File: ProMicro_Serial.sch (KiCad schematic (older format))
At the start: 48 parts, among them J1 USB_C_Receptacle_USB2.0, J2 Conn_01x06, U1 FT232H, U2 93CxxB, Y1 12Mhz

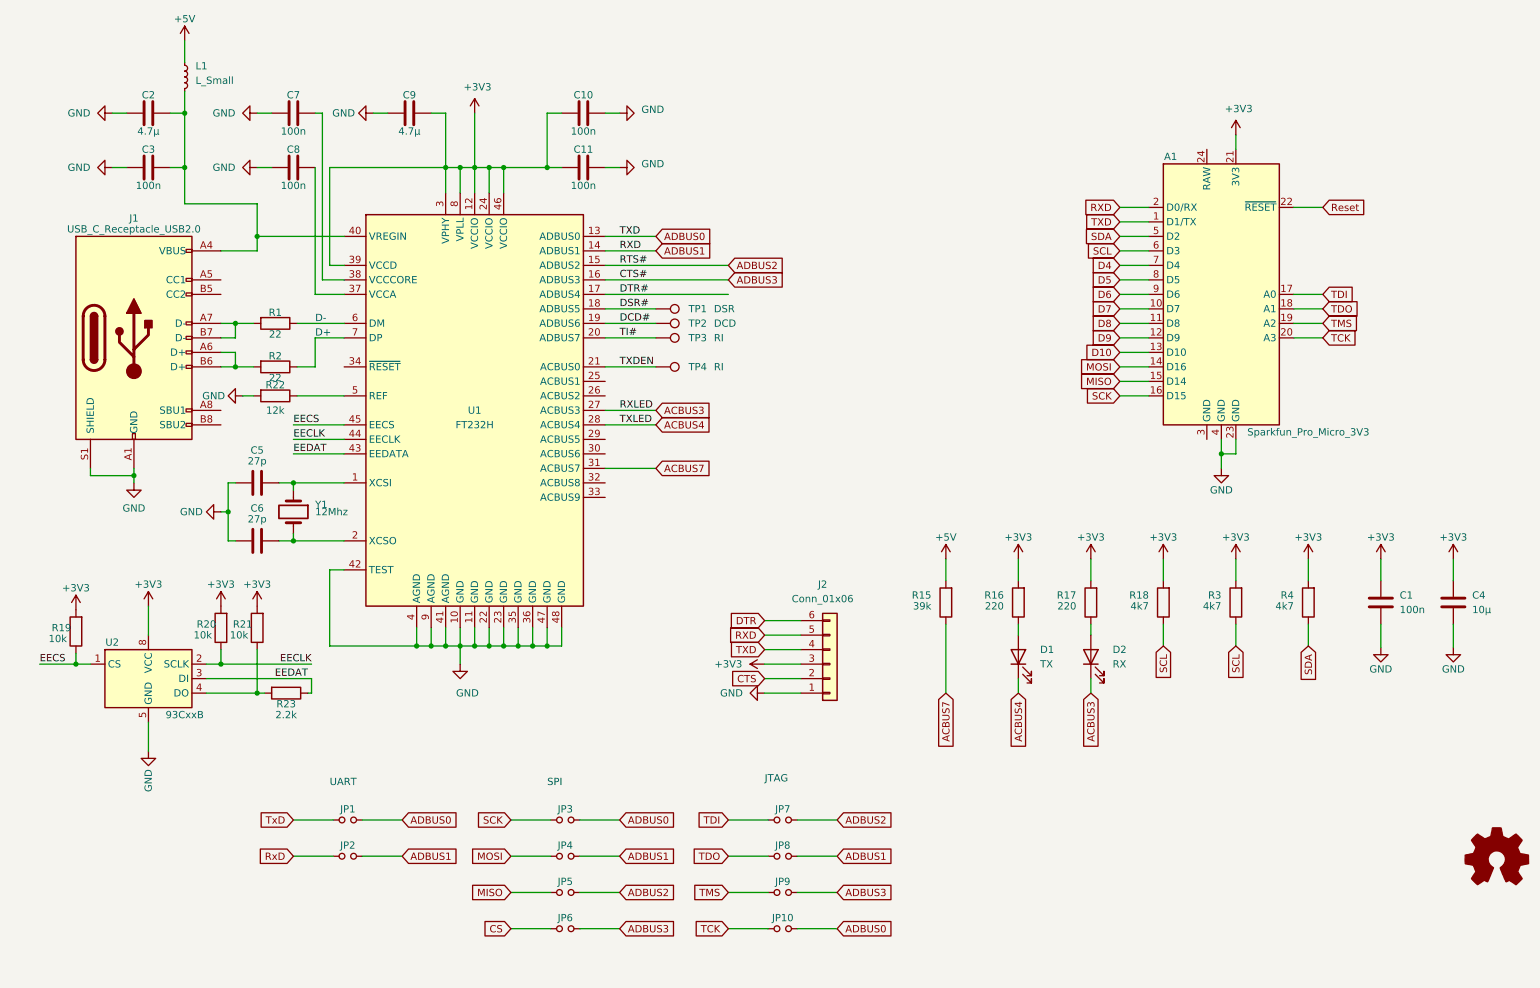
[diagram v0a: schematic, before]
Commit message: schematic, placed parts
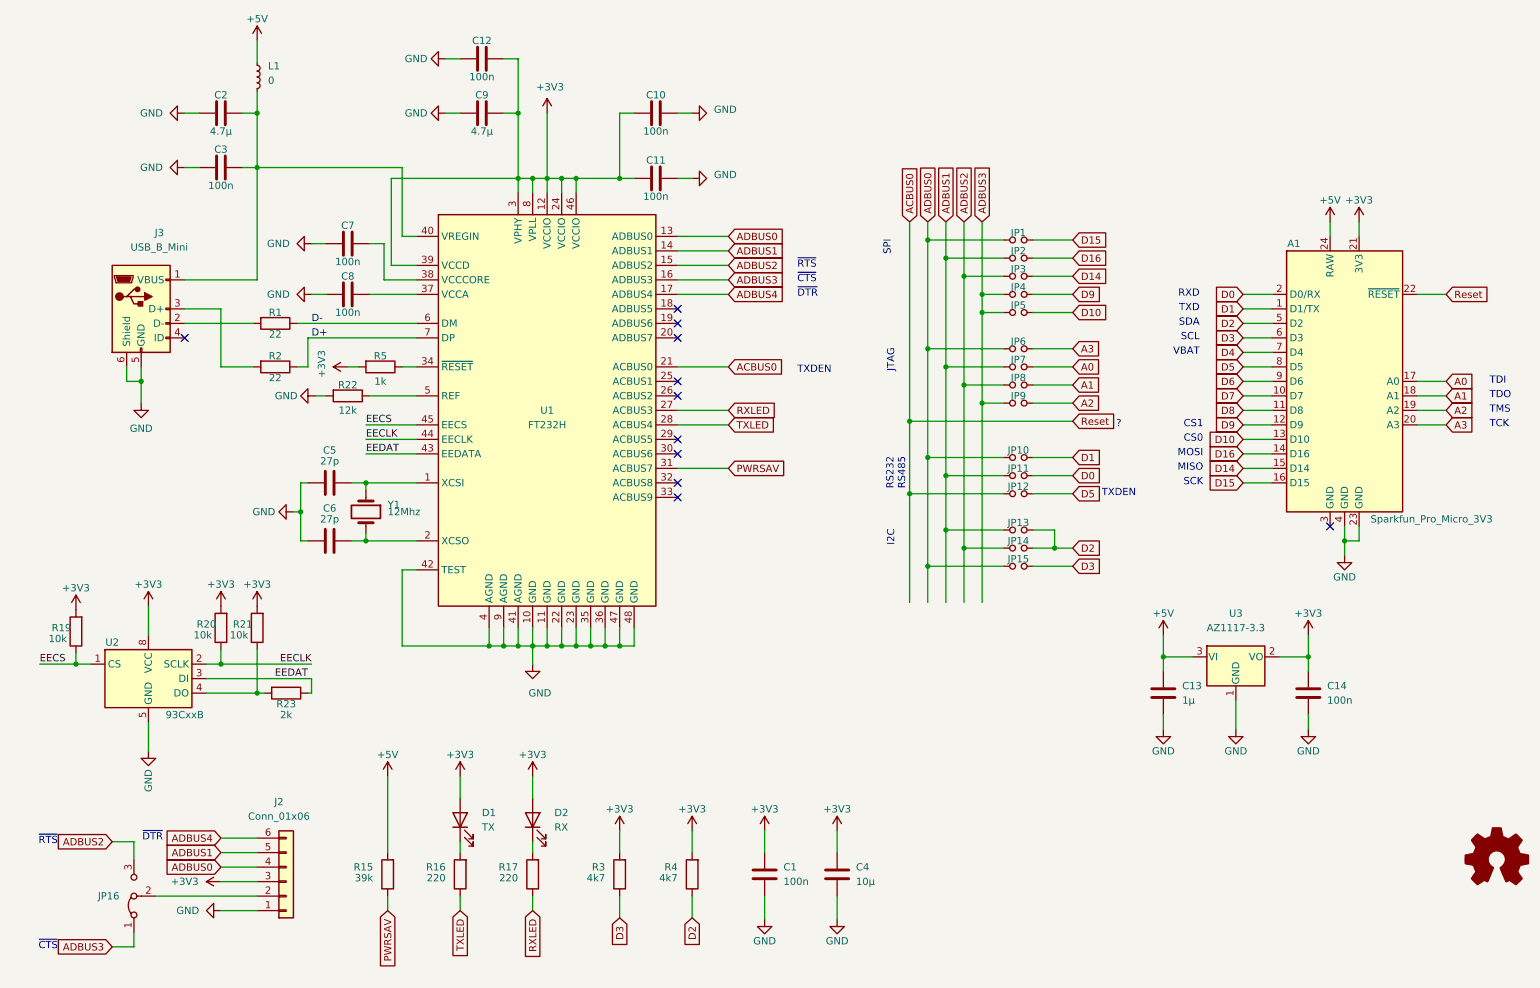
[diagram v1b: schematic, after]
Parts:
- removed J1: USB_C_Receptacle_USB2.0, Connector_USB:USB_C_Receptacle_HRO_TYPE-C-31-M-12, symbol Connector:USB_C_Receptacle_USB2.0
- removed R18: 4k7, Resistor_SMD:R_0402_1005Metric, symbol Device:R
- removed TP1: DSR, symbol Connector:TestPoint
- removed TP2: DCD, symbol Connector:TestPoint
- removed TP3, TP4: RI, symbol Connector:TestPoint
- added C12: 100n, Capacitor_SMD:C_0402_1005Metric, symbol Device:C
- added C13: 1µ, Capacitor_SMD:C_0603_1608Metric, symbol Device:C
- added C14: 100n, Capacitor_SMD:C_0603_1608Metric, symbol Device:C
- added J3: USB_B_Mini, Connector_USB:USB_Mini-B_Wuerth_65100516121_Horizontal, symbol Connector:USB_B_Mini
- added JP11, JP12, JP13, JP14, JP15: Jumper_NO_Small, Jumper:SolderJumper-2_P1.3mm_Open_RoundedPad1.0x1.5mm, symbol Device:Jumper_NO_Small
- added JP16: Jumper_3_Bridged12, Jumper:SolderJumper-3_P1.3mm_Bridged12_RoundedPad1.0x1.5mm, symbol Jumper:Jumper_3_Bridged12
- added R5: 1k, Resistor_SMD:R_0402_1005Metric, symbol Device:R
- added U3: AZ1117-3.3, Package_TO_SOT_SMD:SOT-23-5, symbol Regulator_Linear:AZ1117-3.3
- C11: footprint Capacitor_SMD:C_0603_1608Metric -> Capacitor_SMD:C_0402_1005Metric
- C4: footprint Capacitor_SMD:C_0402_1005Metric -> Capacitor_SMD:C_0603_1608Metric
- L1: value L_Small -> 0; footprint (none) -> Inductor_SMD:L_0603_1608Metric
- LOGO1: footprint Symbol:OSHW-Logo_7.5x8mm_SilkScreen -> Symbol:OSHW-Logo_5.7x6mm_SilkScreen
- R23: value 2.2k -> 2k
- U2: footprint Package_TO_SOT_SMD:SOT-23-6 -> Package_SO:MSOP-8_3x3mm_P0.65mm
- Y1: footprint (none) -> Crystal:Crystal_SMD_3215-2Pin_3.2x1.5mm
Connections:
- net CS is gone; now on net ADBUS0: JP6.1
- net DTR# is gone; now on net ADBUS4: U1.17 (ADBUS4)
- net RxD is gone; now on net ADBUS1: JP2.1
- net TXDEN is gone; now on net ACBUS0: U1.21 (ACBUS0)
- net TxD is gone; now on net ADBUS0: JP1.1
- net +3V3: now also D1.2 (A), D2.2 (A), C12.1, C14.1, R5.2, U3.2 (VO); no longer R16.2, R17.2
- net +5V: now also A1.24 (RAW), C13.1, U3.3 (VI)
- net ADBUS0: now also JP10.1, JP15.1; no longer A1.1 (D1/TX), JP1.2, JP10.2, JP3.2
- net ADBUS1: now also JP7.1, JP11.1, JP13.1; no longer A1.2 (D0/RX), JP2.2, JP4.2, JP8.2
- net ADBUS2: now also JP3.1, JP8.1, JP14.1, JP16.3 (B); no longer JP5.2, JP7.2
- net ADBUS3: now also JP4.1, JP5.1, JP9.1, JP16.1 (A); no longer JP6.2, JP9.2
- net D10: now also JP5.2
- net D5: now also JP12.2
- net D9: now also JP4.2
- net GND: now also C12.2, C13.2, C14.2, J3.5 (GND), J3.6 (Shield), U3.1 (GND)
- net at U1.34 (~RESET): now also R5.1
- net at C2.1, C3.1, L1.2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: now also J3.1 (VBUS)
- net at R2.2: now also J3.3 (D+)
- net at R1.2: now also J3.2 (D-)
- net RXLED: now reaches R17.1
- net RXLED: now also U1.27 (ACBUS3); no longer D2.2 (A)
- net TXLED: now reaches R16.1
- net TXLED: now also U1.28 (ACBUS4); no longer D1.2 (A)
- net ACBUS3: no longer names the net of D2.1 (K)
- net ACBUS3: now also R17.2; no longer U1.27 (ACBUS3)
- net ACBUS4: no longer names the net of D1.1 (K)
- net ACBUS4: now also R16.2; no longer U1.28 (ACBUS4)
- net ACBUS7 renamed PWRSAV
- net CTS: no longer names the net of J2.2 (Pin_2)
- net CTS: now also JP16.2 (C)
- net DCD#: no longer names the net of U1.19 (ADBUS6)
- net DSR#: no longer names the net of U1.18 (ADBUS5)
- net DTR renamed ADBUS4
- net MISO renamed D14
- net D14: now also JP3.2; no longer JP5.1
- net MOSI renamed D16
- net D16: now also JP2.2; no longer JP4.1
- net Reset renamed ACBUS0
- net ACBUS0: now also JP12.1
- net SCK renamed D15
- net D15: now also JP1.2; no longer JP3.1
- net SCL renamed D3
- net D3: now also JP15.2
- net SDA renamed D2
- net D2: now also JP13.2, JP14.2
- net TCK renamed A3
- net A3: now also JP6.2; no longer JP10.1
- net TDI renamed A0
- net A0: now also JP7.2; no longer JP7.1
- net TDO renamed A1
- net A1: now also JP8.2; no longer JP8.1
- net TI#: no longer names the net of U1.20 (ADBUS7)
- net TMS renamed A2
- net A2: now also JP9.2; no longer JP9.1
- new net D0: A1.2 (D0/RX), JP11.2
- new net D1: A1.1 (D1/TX), JP10.2
- no-connect marks 0 -> 11
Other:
- note added: "?"
- note added: "CS0"
- note added: "CS1"
- note added: "I2C"
- note added: "MISO"
- note added: "MOSI"
- note added: "RS232\nRS485"
- note added: "RXD"
- note added: "SCK"
- note added: "SCL"
- note added: "SDA"
- note added: "TCK"
- note added: "TDI"
- note added: "TDO"
- note added: "TMS"
- note added: "TXD"
- note added: "TXDEN"
- note added: "VBAT"
- note added: "~CTS"
- note added: "~DTR"
- note added: "~RTS"
- note removed: "UART"
- moved on the sheet: A1, C1, C10, C11, C2, C3, C4, C5, C6, C7, C8, C9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
